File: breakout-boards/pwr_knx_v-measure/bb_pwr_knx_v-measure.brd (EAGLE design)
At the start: 28.5 x 25 mm, 48 parts, among them IC100 BD9G101, T1 BC856, T2 BCP52, T3 BC847

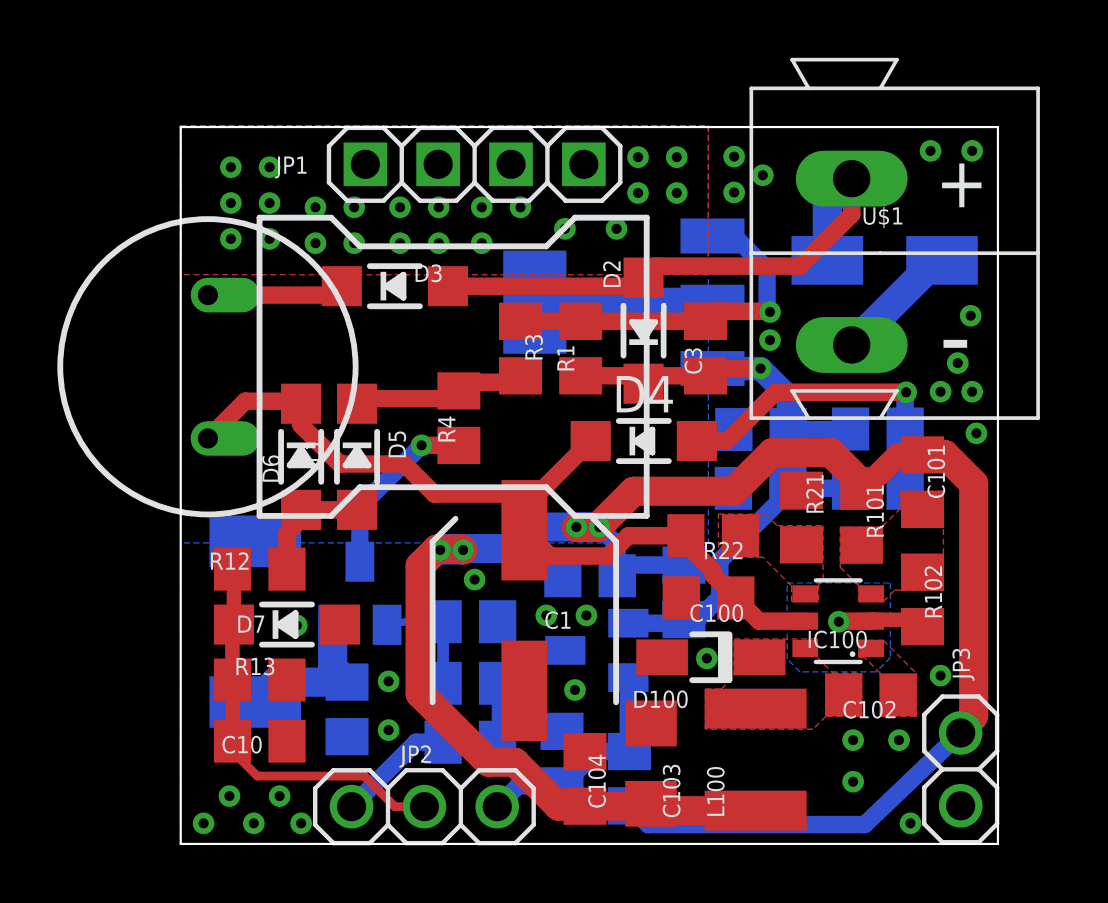
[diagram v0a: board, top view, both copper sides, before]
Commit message: [BB_Pwr+KNX] - removed v-split at buck's enable pin
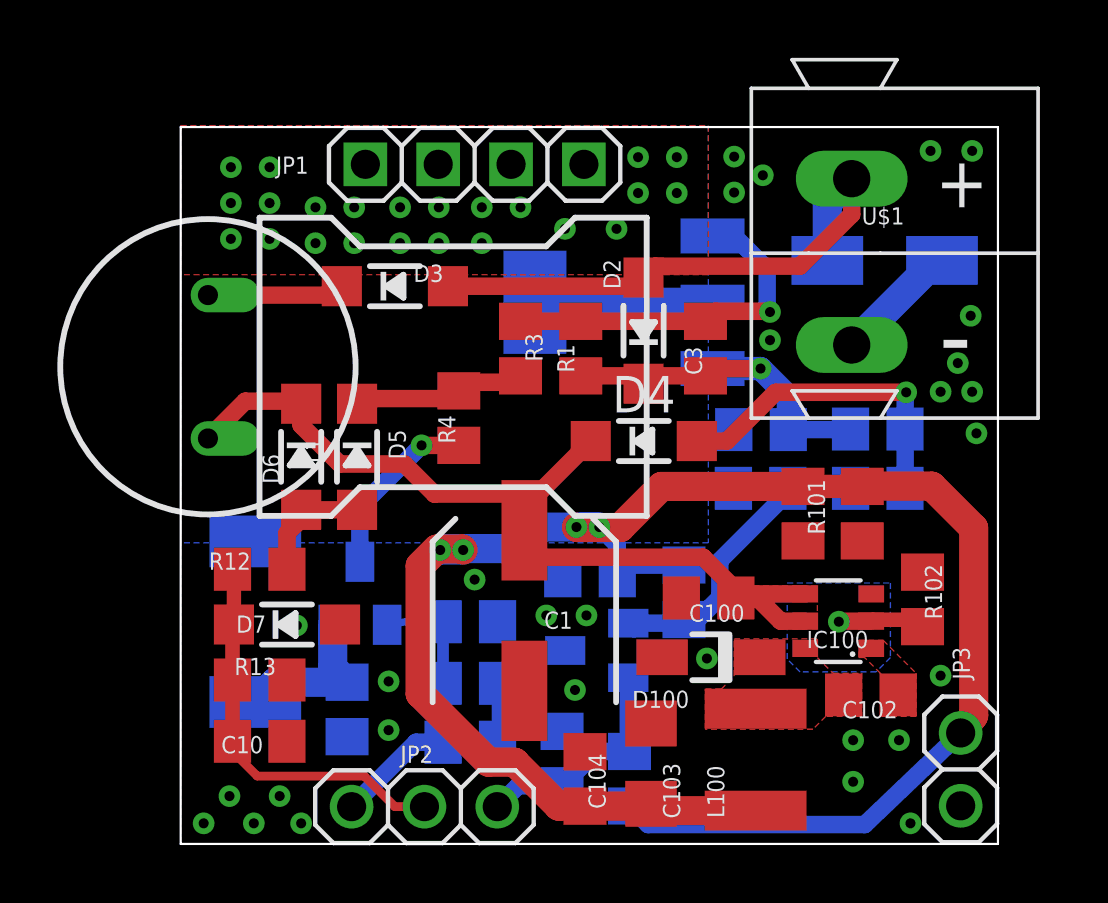
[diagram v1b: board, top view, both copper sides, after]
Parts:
- removed R21: VSplit2, rcl:R0805
- removed R22: VSplit1, rcl:R0805
- moved C101 2.37 mm to (25.3, 11.5)
- moved R101 2.06 mm to (23.2, 11.5)
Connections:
- removed net N$5: IC100.4, R21.1, R22.2
- net EIB_DC: now also IC100.4; no longer R22.1
- net GND: no longer R21.2
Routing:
- net +3V3: track 70.1 -> 67.1 mm
- net EIB_DC: track 34.0 -> 35.6 mm
- added copper zone on layer 1, net EIB_DC
- removed copper zone on layer 1, net FB
- removed copper zone on layer 1, net N$5

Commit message: [BB_Pwr+KNX] removed attributes, switched to 2x47uF mlccs
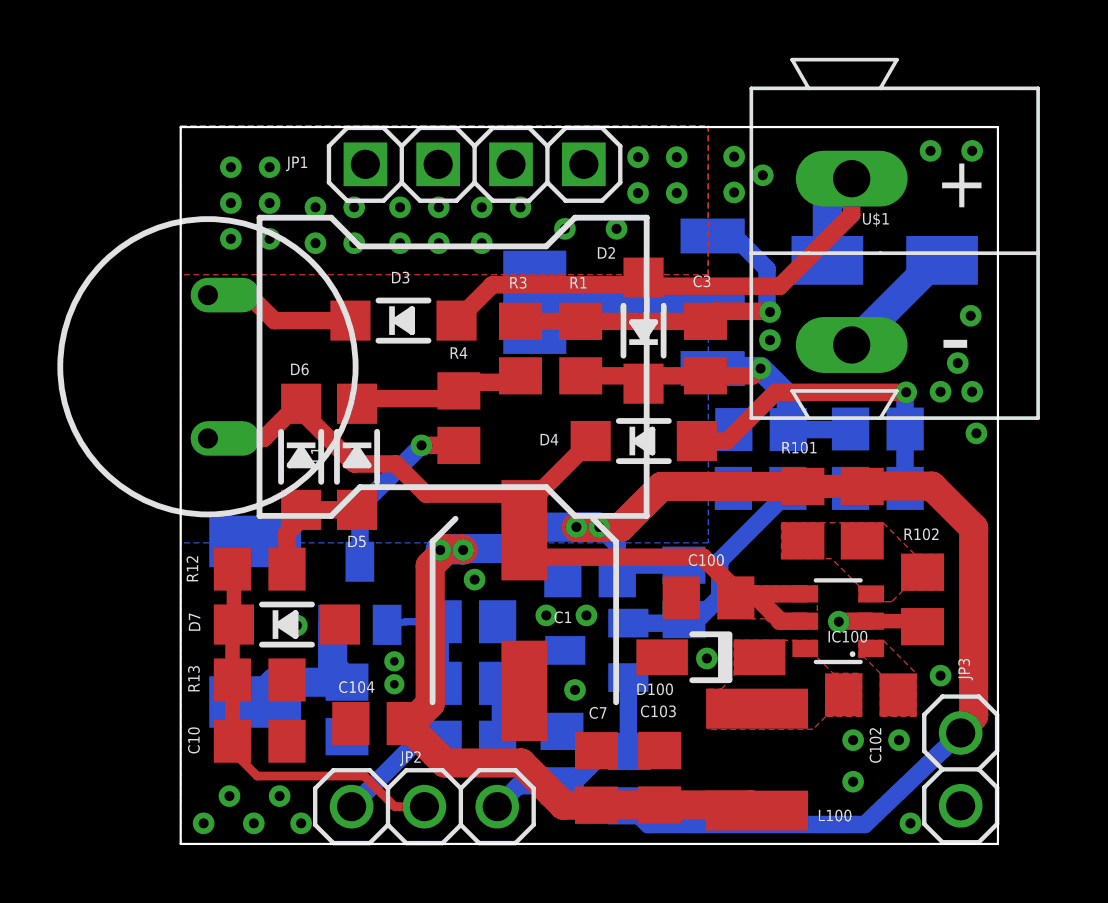
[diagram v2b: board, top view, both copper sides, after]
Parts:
- added C7: 47u 10V, rcl:C0805
- C103: value 22µ/25V -> 47u 10V; device rcl:C1206 -> rcl:C0805
- moved C104 7.47 mm to (8.38, 4.20), turned to 180 degrees
- moved D3 1.24 mm to (9.27, 18.2)
- moved C103 0.58 mm to (18.2, 2.31)
- moved L100 0.05 mm to (21.6, 2.94)
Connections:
- net +3V3: now also C7.1
- net GND: now also C7.2
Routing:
- net EIB_DC: track 35.6 -> 32.4 mm
- net +3V3: track 67.1 -> 68.3 mm
- net N$2: track 4.80 -> 5.34 mm
- added copper zone on layer 1, net FB
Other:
- board text added: "https://selfbus.org Power and KNX-Connection Board v0.9.0"
- board text removed: "Selfbus Power and KNX-Connection Board v0.8.0"

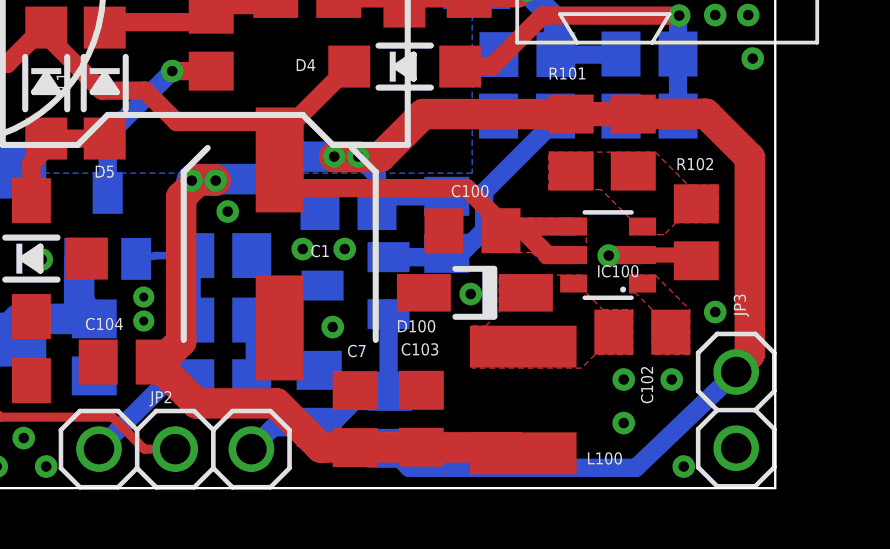
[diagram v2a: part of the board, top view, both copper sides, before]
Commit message: [BB_Pwr+KNX] - changed values to standard values
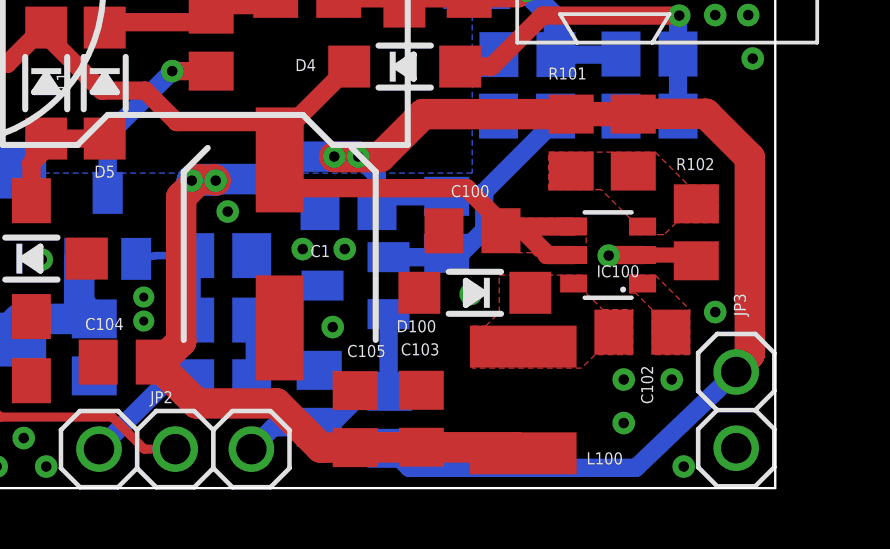
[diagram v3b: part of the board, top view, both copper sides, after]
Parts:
- C1: value 100µ/35V -> 100uF 35V
- C10, C2, C6: value 100n -> 100nF
- C100: value 4.7µF/50V -> 4.7uF 50V
- C101: value 270n -> 270nF
- C103, C105: value 47u 10V -> 47uF 10V
- C3, C4: value 10n -> 10nF
- C5: value 100p -> 100pF
- D100: device bt_diode:SOD123FL -> microbuilder:SOD-123
- L100: value 6.8µH -> 6.8uH
- R101: value 2k4 -> 1k6
- R102: value 680R -> 470R
- renumbered C7 to C105

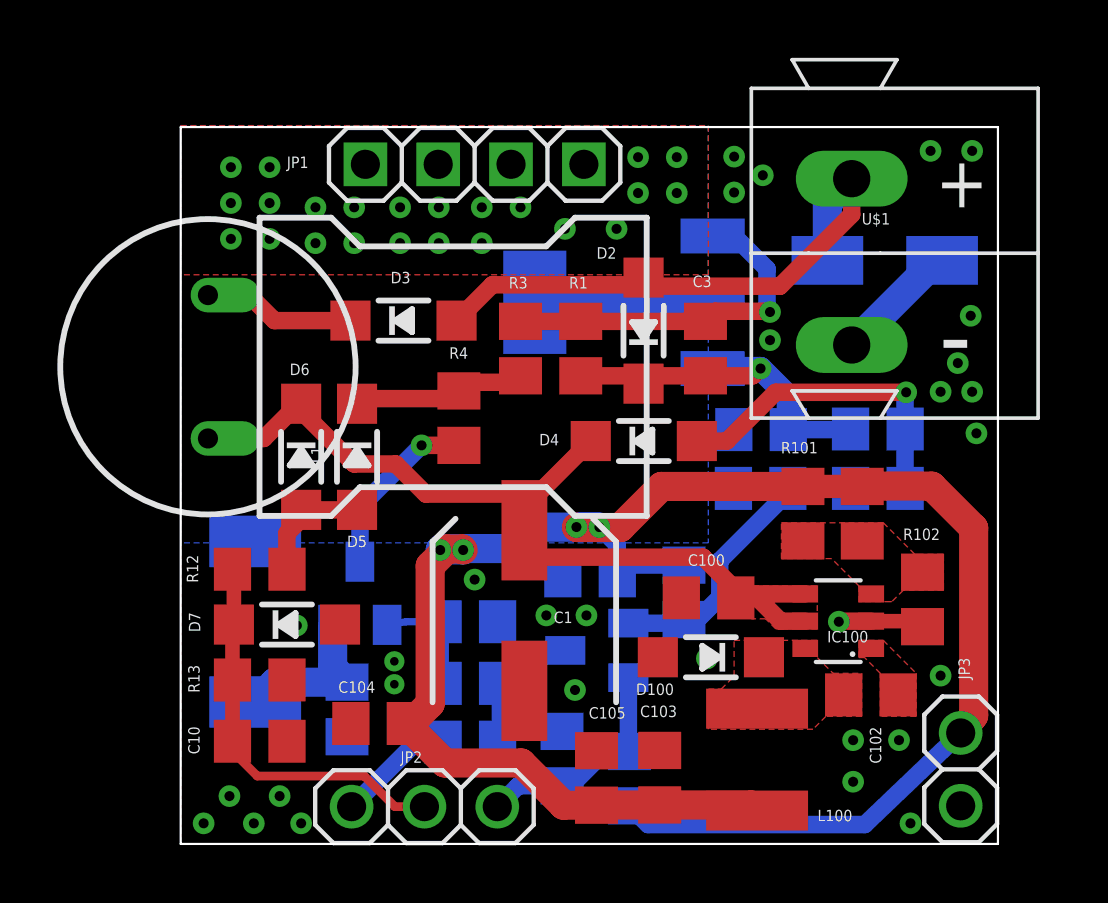
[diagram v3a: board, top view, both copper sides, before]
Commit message: [BB_Pwr+KNX] - update pin positions
accidentially committed a version with old pin positions yesterday
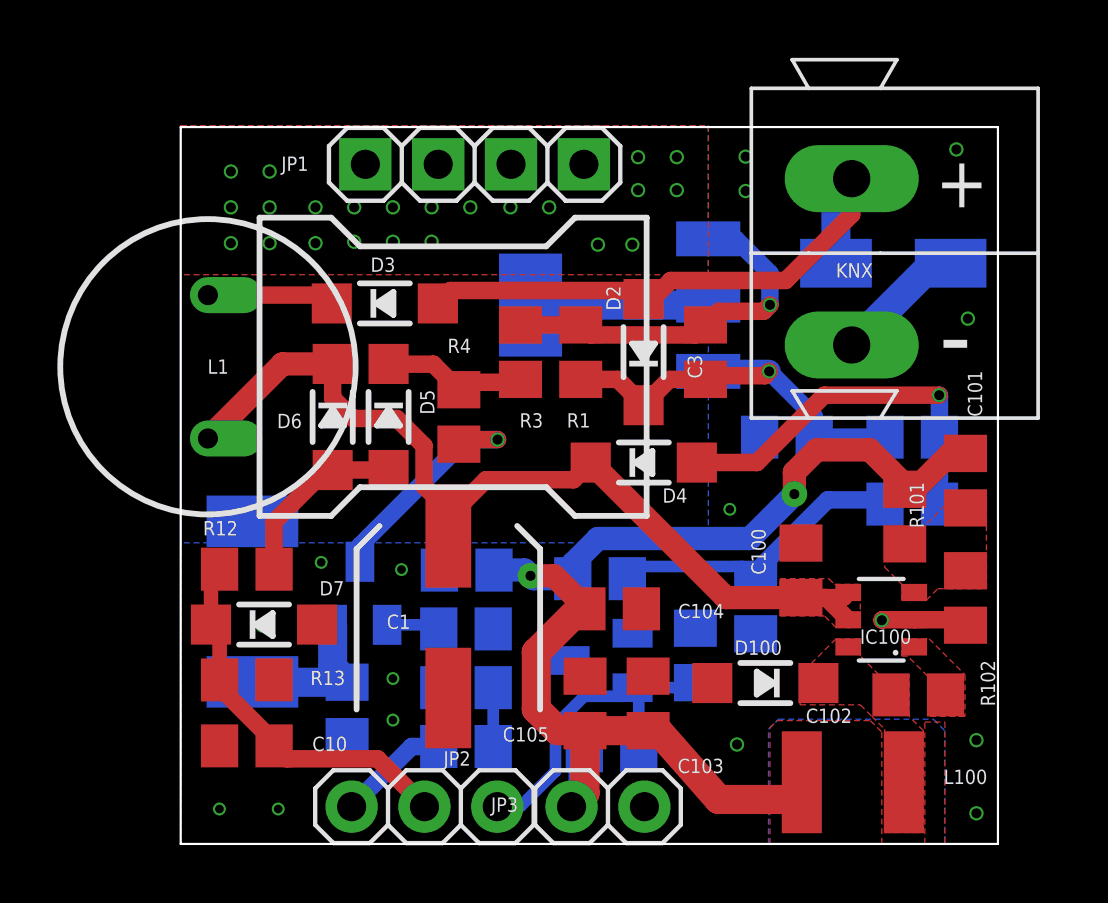
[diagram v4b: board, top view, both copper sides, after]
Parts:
- C1: value 100uF 35V -> 100µ/35V
- C10, C2, C6: value 100nF -> 100n
- C101: value 270nF -> 270n
- C3, C4: value 10nF -> 10n
- C5: value 100pF -> 100p
- D7: value DDZ9685 -option -> DDZ9685
- R101: value 1k6 -> 2k4
- R102: value 470R -> 680R
- R25: value 24R 1210/0.5W -> 24R 2512/1.0W
- R9: value 47k -> 100k
- moved JP3 12.4 mm to (16.4, 1.30), turned to 0 degrees
- moved C104 9.15 mm to (16.6, 8.20), turned to 0 degrees
- moved C5 5.88 mm to (19.4, 6.58)
- moved C6 4.30 mm to (11.5, 9.55)
- moved R9 4.13 mm to (21.6, 8.28), turned to 90 degrees
- moved C101 3.78 mm to (28.9, 12.7)
- moved R101 3.55 mm to (26.8, 11.4)
- moved L100 3.43 mm to (24.9, 2.15), turned to 180 degrees
- moved C100 3.36 mm to (23.1, 9.54), turned to 270 degrees
- moved R8 2.96 mm to (16.1, 9.25), turned to 0 degrees
- moved C1 2.66 mm to (10.8, 7.89)
- moved C105 2.63 mm to (15.6, 4.90)
- moved C103 2.62 mm to (17.8, 4.90)
- moved D100 2.10 mm to (21.9, 5.61)
- moved D5 1.77 mm to (8.75, 14.9)
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- renumbered U$1 to KNX
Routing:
- net +3V3: track 68.3 -> 43.2 mm, vias 4 -> 2
- net EIB_IN: track 8.04 -> 11.9 mm
- net N$14: track 10.5 -> 12.8 mm
- net N$6: track 6.25 -> 8.31 mm
- net REF: track 4.36 -> 6.39 mm
- net EIB+DIR: track 13.0 -> 15.0 mm
- net N$1: track 11.4 -> 13.2 mm
- net N$25: track 6.21 -> 5.13 mm
- net EIB_DC: track 32.4 -> 33.5 mm
- net N$2: track 5.34 -> 4.44 mm
- net N$8: track 7.07 -> 6.20 mm
- net EIB+: track 20.0 -> 20.7 mm
- net BUS_V: track 13.9 -> 13.3 mm
- net GND: track 7.38 -> 7.64 mm, vias 30 -> 16
- added copper zone on layer 1, net NOGND
- added copper zone on layer 16, net NOGND1
- added copper zone on layer 1, net NOGND2
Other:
- board text added: "Selfbus Power and KNX-Connection Board v0.9.1"
- board text removed: "https://selfbus.org Power and KNX-Connection Board v0.9.0"

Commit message: [BB_Pwr+KNX] - updated docu; updated values of buck components
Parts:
- C1: value 100µ/35V -> 100uF 35V
- C101: value 270n -> 470nF
- C104: value 100n -> 100nF
- L100: value 6.8uH -> 4.7uH
- R101: value 2k4 -> 1k6
- R102: value 680R -> 470R
- R25: value 24R 2512/1.0W -> 24R 2512 1.0W
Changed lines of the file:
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@@
 <layer number="25" name="tNames" color="7" fill="1" visible="yes" active="yes"/>
 <layer number="26" name="bNames" color="7" fill="1" visible="no" active="yes"/>
-<layer number="27" name="tValues" color="7" fill="1" visible="no" active="yes"/>
+<layer number="27" name="tValues" color="7" fill="1" visible="yes" active="yes"/>
 <layer number="28" name="bValues" color="7" fill="1" visible="no" active="yes"/>
 <layer number="29" name="tStop" color="7" fill="3" visible="no" active="yes"/>
@@
 </layers>
 <board>
-<fusionsync huburn="a.YnVzaW5lc3M6bXlnbXgyNDY1Mw" projecturn="a.YnVzaW5lc3M6bXlnbXgyNDY1MyMyMDIxMDMyODM5NzU1Njk4MQ" f3durn="urn:adsk.wipprod:dm.lineage:0cTEfbg9Tti8mzLoLkRzTg" pcbguid="" lastpulledtime="" lastsyncedchangeguid="" latestrevisionid="eed3cd53-31b2-4d0b-acc2-1091cec6bf2a" lastsyncedrevisionid="eed3cd53-31b2-4d0b-acc2-1091cec6bf2a" lastboardhashguid="30e0524a-6a2e-eb4e-3ab6-5c9ec57f5a7d" lastpushedtime="2023-02-09T19:20:59Z" linktopcb3d="true"/>
+<fusionsync huburn="a.YnVzaW5lc3M6bXlnbXgyNDY1Mw" projecturn="a.YnVzaW5lc3M6bXlnbXgyNDY1MyMyMDIxMDMyODM5NzU1Njk4MQ" f3durn="urn:adsk.wipprod:dm.lineage:0cTEfbg9Tti8mzLoLkRzTg" pcbguid="" lastpulledtime="" lastsyncedchangeguid="" latestrevisionid="eed3cd53-31b2-4d0b-acc2-1091cec6bf2a" lastsyncedrevisionid="eed3cd53-31b2-4d0b-acc2-1091cec6bf2a" lastboardhashguid="30e0524a-6a2e-eb4e-3ab6-5c9ec57f5a7d" lastpushedtime="2023-02-09T19:20:59Z" linktopcb3d="false"/>
 <plain>
 <polygon width="0.1524" layer="20">
@@
 </autorouter>
 <elements>
-<element name="C104" library="rcl" library_urn="urn:adsk.eagle:library:334" package="C0805" package3d_urn="urn:adsk.eagle:package:23617/2" value="100n" x="16.616" y="8.2" smashed="yes">
+<element name="C104" library="rcl" library_urn="urn:adsk.eagle:library:334" package="C0805" package3d_urn="urn:adsk.eagle:package:23617/2" value="100nF" x="16.616" y="8.2" smashed="yes">
 <attribute name="NAME" x="18.846" y="7.87" size="0.5" layer="25"/>
 <attribute name="POPULARITY" value="88" x="16.616" y="8.2" size="1.778" layer="27" display="off"/>
@@
 <attribute name="VALUE" x="29.552" y="12.122" size="0.5" layer="27" ratio="10" rot="R90"/>
 </element>
-<element name="L100" library="rcl_changed" package="L4532P" package3d_urn="urn:adsk.eagle:package:23484/1" value="6.8uH" x="24.9387" y="2.15" smashed="yes" rot="R180">
+<element name="L100" library="rcl_changed" package="L4532P" package3d_urn="urn:adsk.eagle:package:23484/1" value="4.7uH" x="24.9387" y="2.15" smashed="yes" rot="R180">
 <attribute name="NAME" x="28.1063" y="2.09" size="0.5" layer="25"/>
 <attribute name="POPULARITY" value="0" x="24.9387" y="2.15" size="1.778" layer="27" rot="R180" display="off"/>
@@
 <attribute name="VALUE" x="28" y="6.041" size="0.5" layer="27" rot="R180"/>
 </element>
-<element name="R101" library="rcl" library_urn="urn:adsk.eagle:library:334" package="R0805" package3d_urn="urn:adsk.eagle:package:23553/2" value="2k4" x="26.75" y="11.41725" smashed="yes" rot="R90">
+<element name="R101" library="rcl" library_urn="urn:adsk.eagle:library:334" package="R0805" package3d_urn="urn:adsk.eagle:package:23553/2" value="1k6" x="26.75" y="11.41725" smashed="yes" rot="R90">
 <attribute name="NAME" x="26.92" y="12.61775" size="0.5" layer="25" rot="R270"/>
 <attribute name="POPULARITY" value="86" x="26.75" y="11.41725" size="1.778" layer="27" rot="R90" display="off"/>
@@
 <attribute name="VALUE" x="26.01" y="12.46775" size="0.5" layer="27" rot="R270"/>
 </element>
-<element name="R102" library="rcl" library_urn="urn:adsk.eagle:library:334" package="R0805" package3d_urn="urn:adsk.eagle:package:23553/2" value="680R" x="28.87" y="8.577" smashed="yes" rot="R90">
+<element name="R102" library="rcl" library_urn="urn:adsk.eagle:library:334" package="R0805" package3d_urn="urn:adsk.eagle:package:23553/2" value="470R" x="28.87" y="8.577" smashed="yes" rot="R90">
 <attribute name="NAME" x="29.4" y="6.408" size="0.5" layer="25" rot="R270"/>
 <attribute name="POPULARITY" value="86" x="28.87" y="8.577" size="1.778" layer="27" rot="R90" display="off"/>
@@
 <attribute name="VALUE" x="28.14" y="9.708" size="0.5" layer="27" rot="R270"/>
 </element>
-<element name="C101" library="rcl" library_urn="urn:adsk.eagle:library:334" package="C0805" package3d_urn="urn:adsk.eagle:package:23617/2" value="270n" x="28.869" y="12.66725" smashed="yes" rot="R90">
+<element name="C101" library="rcl" library_urn="urn:adsk.eagle:library:334" package="C0805" package3d_urn="urn:adsk.eagle:package:23617/2" value="470nF" x="28.869" y="12.66725" smashed="yes" rot="R90">
 <attribute name="NAME" x="29.449" y="14.89725" size="0.5" layer="25" rot="R90"/>
 <attribute name="POPULARITY" value="88" x="28.869" y="12.66725" size="1.778" layer="27" rot="R90" display="off"/>
@@
 <attribute name="VALUE" x="12.985" y="5.26" size="0.5" layer="28" rot="MR0"/>
 </element>
-<element name="C1" library="rcl" library_urn="urn:adsk.eagle:library:334" package="SANYO-OSCON_SMD_C6" package3d_urn="urn:adsk.eagle:package:23465/1" value="100µ/35V" x="10.834" y="7.889" smashed="yes" rot="R90">
+<element name="C1" library="rcl" library_urn="urn:adsk.eagle:library:334" package="SANYO-OSCON_SMD_C6" package3d_urn="urn:adsk.eagle:package:23465/1" value="100uF 35V" x="10.834" y="7.889" smashed="yes" rot="R90">
 <attribute name="NAME" x="8.686" y="7.498" size="0.5" layer="25"/>
 <attribute name="POPULARITY" value="0" x="10.834" y="7.889" size="1.778" layer="27" rot="R90" display="off"/>
@@
 <element name="D3" library="microbuilder" package="SOD-123" value="1N4148" x="8.619" y="18.85" smashed="yes">
 <attribute name="NAME" x="8.119" y="19.95" size="0.5" layer="25"/>
-<attribute name="REICHELT" value="1N 4148 SMD" x="8.619" y="18.85" size="1.016" layer="27" display="off"/>
 <attribute name="VALUE" x="7.519" y="17.3" size="0.5" layer="27"/>
 </element>
@@
 <attribute name="VALUE" x="23.4" y="19.162" size="0.5" layer="27"/>
 </element>
-<element name="R25" library="rcl" library_urn="urn:adsk.eagle:library:334" package="R2512" package3d_urn="urn:adsk.eagle:package:23545/2" value="24R  2512/1.0W" x="4" y="8.45" smashed="yes" rot="MR90">
+<element name="R25" library="rcl" library_urn="urn:adsk.eagle:library:334" package="R2512" package3d_urn="urn:adsk.eagle:package:23545/2" value="24R  2512 1.0W" x="4" y="8.45" smashed="yes" rot="MR90">
 <attribute name="NAME" x="4.59" y="3.755" size="0.5" layer="26" rot="MR0"/>
 <attribute name="POPULARITY" value="0" x="4" y="8.45" size="1.778" layer="28" rot="MR90" display="off"/>
